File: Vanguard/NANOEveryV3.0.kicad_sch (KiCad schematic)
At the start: 57 parts, among them IC1 MPM3610, J1 -, J2 DNP, Q1 BSS138PS, Q2 BSS138PS, Q3 BSS138, U1 ATMEGA4809, U2 AP2112K-3.3, U3 ATSAMD11D14A, U4 ICM-20602

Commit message: (almost done) with the footprints
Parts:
- FD1, FD2: footprint NANOEveryV3.0:FD-1-1.5 -> TestPoint:TestPoint_THTPad_1.0x1.0mm_Drill0.5mm
- J1: footprint NANOEveryV3.0:ZX62-AB-5PA -> Connector_USB:USB_Micro-AB_Molex_47590-0001
- J2: footprint NANOEveryV3.0:2X03-TP -> Connector_PinHeader_1.00mm:PinHeader_2x03_P1.00mm_Vertical
- JP2: footprint NANOEveryV3.0:1X15-CASTELL -> Connector_PinHeader_1.00mm:PinHeader_1x15_P1.00mm_Vertical_SMD_Pin1Left
- JP3: footprint NANOEveryV3.0:1X15-CASTELL -> Connector_PinHeader_1.00mm:PinHeader_1x15_P1.00mm_Vertical_SMD_Pin1Right
- PB1: footprint NANOEveryV3.0:C&K_PTS820_NO_HOLES -> Button_Switch_SMD:SW_Tactile_SPST_NO_Straight_CK_PTS636Sx25SMTRLFS
- Q1, Q2: footprint NANOEveryV3.0:SOT363 -> Package_TO_SOT_SMD:SOT-363_SC-70-6
- R1, R10, R11, R12, R13, R14, R15, R16, R17, R18, R19, R2, R3, R4, R5, R6, R7, R8, R9: footprint NANOEveryV3.0:0402-1005X55N -> Resistor_SMD:R_0402_1005Metric
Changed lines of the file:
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@@
 			)
 		)
-		(property "Footprint" "NANOEveryV3.0:0402-1005X55N"
+		(property "Footprint" "Resistor_SMD:R_0402_1005Metric"
 			(at 187.96 97.79 0)
 			(effects
@@
 			)
 		)
-		(property "Footprint" "NANOEveryV3.0:0402-1005X55N"
+		(property "Footprint" "Resistor_SMD:R_0402_1005Metric"
 			(at 229.87 146.05 0)
 			(effects
@@
 			)
 		)
-		(property "Footprint" "NANOEveryV3.0:ZX62-AB-5PA"
+		(property "Footprint" "Connector_USB:USB_Micro-AB_Molex_47590-0001"
 			(at 38.1 110.49 0)
 			(effects
@@
 			)
 		)
-		(property "Footprint" "NANOEveryV3.0:FD-1-1.5"
+		(property "Footprint" "TestPoint:TestPoint_THTPad_1.0x1.0mm_Drill0.5mm"
 			(at 396.24 27.94 0)
 			(effects
@@
 			)
 		)
-		(property "Footprint" "NANOEveryV3.0:0402-1005X55N"
+		(property "Footprint" "Resistor_SMD:R_0402_1005Metric"
 			(at 57.15 153.67 0)
 			(effects
@@
 			)
 		)
-		(property "Footprint" "NANOEveryV3.0:FD-1-1.5"
+		(property "Footprint" "TestPoint:TestPoint_THTPad_1.0x1.0mm_Drill0.5mm"
 			(at 389.89 27.94 0)
 			(effects
@@
 			)
 		)
-		(property "Footprint" "NANOEveryV3.0:0402-1005X55N"
+		(property "Footprint" "Resistor_SMD:R_0402_1005Metric"
 			(at 212.09 146.05 0)
 			(effects
@@
 			)
 		)
-		(property "Footprint" "NANOEveryV3.0:0402-1005X55N"
+		(property "Footprint" "Resistor_SMD:R_0402_1005Metric"
 			(at 35.56 49.53 0)
 			(effects
@@
 			)
 		)
-		(property "Footprint" "NANOEveryV3.0:0402-1005X55N"
+		(property "Footprint" "Resistor_SMD:R_0402_1005Metric"
 			(at 229.87 123.19 0)
 			(effects
@@
 			)
 		)
-		(property "Footprint" "NANOEveryV3.0:2X03-TP"
+		(property "Footprint" "Connector_PinHeader_1.00mm:PinHeader_2x03_P1.00mm_Vertical"
 			(at 71.12 152.4 0)
 			(effects
@@
 			)
 		)
-		(property "Footprint" "NANOEveryV3.0:0402-1005X55N"
+		(property "Footprint" "Resistor_SMD:R_0402_1005Metric"
 			(at 248.92 203.2 0)
 			(effects
@@
 			)
 		)
-		(property "Footprint" "NANOEveryV3.0:SOT363"
+		(property "Footprint" "Package_TO_SOT_SMD:SOT-363_SC-70-6"
 			(at 220.98 133.35 0)
 			(effects
@@
 			)
 		)
-		(property "Footprint" "NANOEveryV3.0:0402-1005X55N"
+		(property "Footprint" "Resistor_SMD:R_0402_1005Metric"
 			(at 205.74 97.79 0)
 			(effects
@@
 			)
 		)
-		(property "Footprint" "NANOEveryV3.0:0402-1005X55N"
+		(property "Footprint" "Resistor_SMD:R_0402_1005Metric"
 			(at 50.8 140.97 0)
 			(effects
@@
 			)
 		)
-		(property "Footprint" "NANOEveryV3.0:0402-1005X55N"
+		(property "Footprint" "Resistor_SMD:R_0402_1005Metric"
 			(at 176.53 152.4 0)
 			(effects
@@
 			)
 		)
-		(property "Footprint" "NANOEveryV3.0:1X15-CASTELL"
+		(property "Footprint" "Connector_PinHeader_1.00mm:PinHeader_1x15_P1.00mm_Vertical_SMD_Pin1Left"
 			(at 317.5 99.06 0)
 			(effects
@@
 			)
 		)
-		(property "Footprint" "NANOEveryV3.0:0402-1005X55N"
+		(property "Footprint" "Resistor_SMD:R_0402_1005Metric"
 			(at 35.56 66.04 0)
 			(effects
@@
 			)
 		)
-		(property "Footprint" "NANOEveryV3.0:0402-1005X55N"
+		(property "Footprint" "Resistor_SMD:R_0402_1005Metric"
 			(at 166.37 152.4 0)
 			(effects
@@
 			)
 		)
-		(property "Footprint" "NANOEveryV3.0:0402-1005X55N"
+		(property "Footprint" "Resistor_SMD:R_0402_1005Metric"
 			(at 181.61 123.19 0)
 			(effects
@@
 			)
 		)
-		(property "Footprint" "NANOEveryV3.0:0402-1005X55N"
+		(property "Footprint" "Resistor_SMD:R_0402_1005Metric"
 			(at 73.66 62.23 0)
 			(effects
@@
 			)
 		)
-		(property "Footprint" "NANOEveryV3.0:0402-1005X55N"
+		(property "Footprint" "Resistor_SMD:R_0402_1005Metric"
 			(at 302.26 74.93 0)
 			(effects
@@
 			)
 		)
-		(property "Footprint" "NANOEveryV3.0:0402-1005X55N"
+		(property "Footprint" "Resistor_SMD:R_0402_1005Metric"
 			(at 73.66 54.61 0)
 			(effects
@@
 			)
 		)
-		(property "Footprint" "NANOEveryV3.0:0402-1005X55N"
+		(property "Footprint" "Resistor_SMD:R_0402_1005Metric"
 			(at 80.01 133.35 0)
 			(effects
@@
 			)
 		)
-		(property "Footprint" "NANOEveryV3.0:SOT363"
+		(property "Footprint" "Package_TO_SOT_SMD:SOT-363_SC-70-6"
 			(at 196.85 107.95 0)
 			(effects
@@
 			)
 		)
-		(property "Footprint" "NANOEveryV3.0:1X15-CASTELL"
+		(property "Footprint" "Connector_PinHeader_1.00mm:PinHeader_1x15_P1.00mm_Vertical_SMD_Pin1Right"
 			(at 327.66 99.06 0)
 			(effects
@@
 			)
 		)
-		(property "Footprint" "NANOEveryV3.0:0402-1005X55N"
+		(property "Footprint" "Resistor_SMD:R_0402_1005Metric"
 			(at 212.09 123.19 0)
 			(effects
@@
 			)
 		)
-		(property "Footprint" "NANOEveryV3.0:0402-1005X55N"
+		(property "Footprint" "Resistor_SMD:R_0402_1005Metric"
 			(at 123.19 55.88 0)
 			(effects
@@
 			)
 		)
-		(property "Footprint" "NANOEveryV3.0:C&K_PTS820_NO_HOLES"
+		(property "Footprint" "Button_Switch_SMD:SW_Tactile_SPST_NO_Straight_CK_PTS636Sx25SMTRLFS"
 			(at 236.22 213.36 0)
 			(effects
@@
 			)
 		)
-		(property "Footprint" "NANOEveryV3.0:SOT363"
+		(property "Footprint" "Package_TO_SOT_SMD:SOT-363_SC-70-6"
 			(at 220.98 156.21 0)
 			(effects

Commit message: Assigned footprints for mpm3610
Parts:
- IC1: footprint NANOEveryV3.0:MPM3610 -> Package_DFN_QFN:DFN-18-1EP_3x5mm_P0.5mm_EP1.66x4.4mm
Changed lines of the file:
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@@
 			)
 		)
-		(property "Footprint" "NANOEveryV3.0:MPM3610"
+		(property "Footprint" "Package_DFN_QFN:DFN-18-1EP_3x5mm_P0.5mm_EP1.66x4.4mm"
 			(at 53.34 50.8 0)
 			(effects

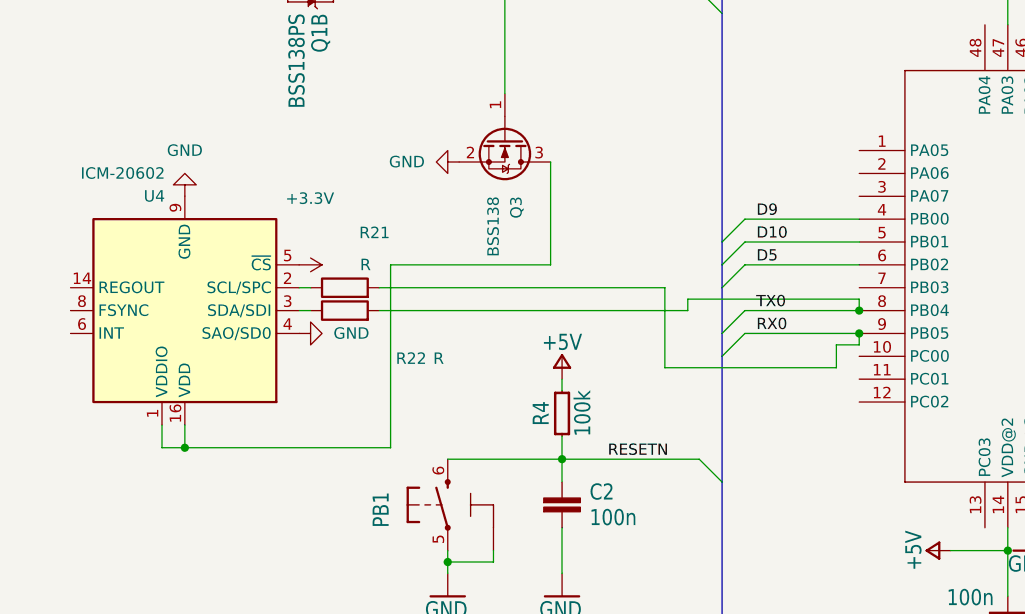
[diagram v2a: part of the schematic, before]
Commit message: Removed connections from icm20602
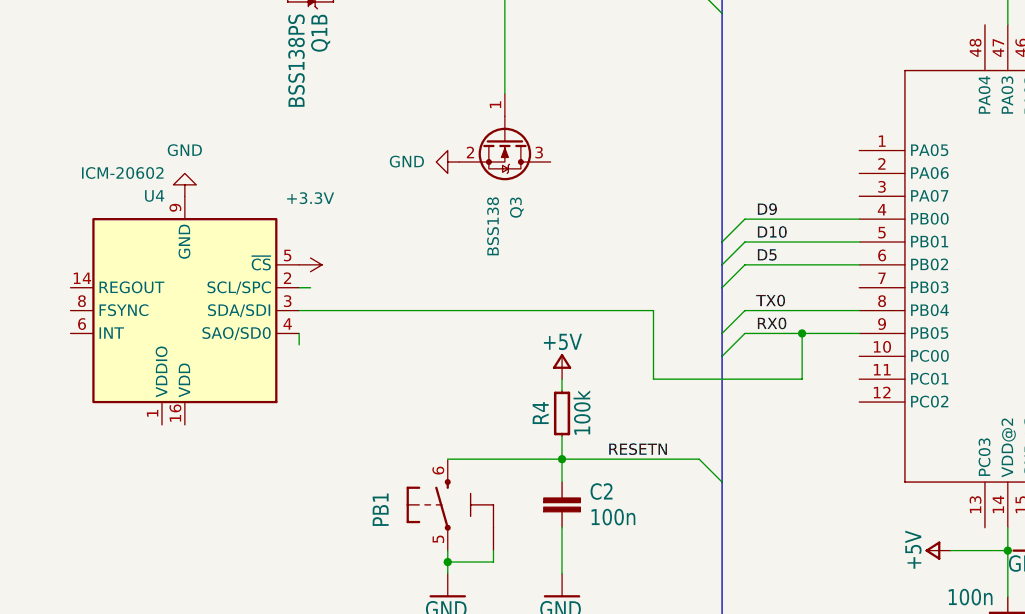
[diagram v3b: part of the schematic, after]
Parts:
- removed R21, R22: R, symbol Device:R
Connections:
- net GND: no longer U4.4 (SAO/SD0)
- net RX0: now also U4.3 (SDA/SDI)
- now unconnected: Q3.3 (D), U4.1 (VDDIO), U4.16 (VDD)

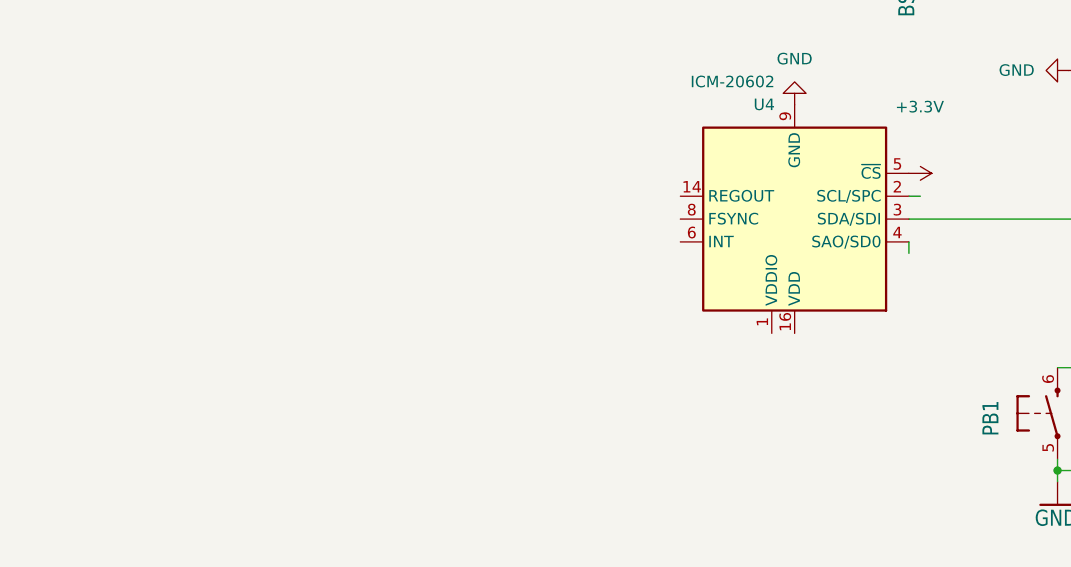
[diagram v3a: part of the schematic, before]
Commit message: Added a Note for icm-20602
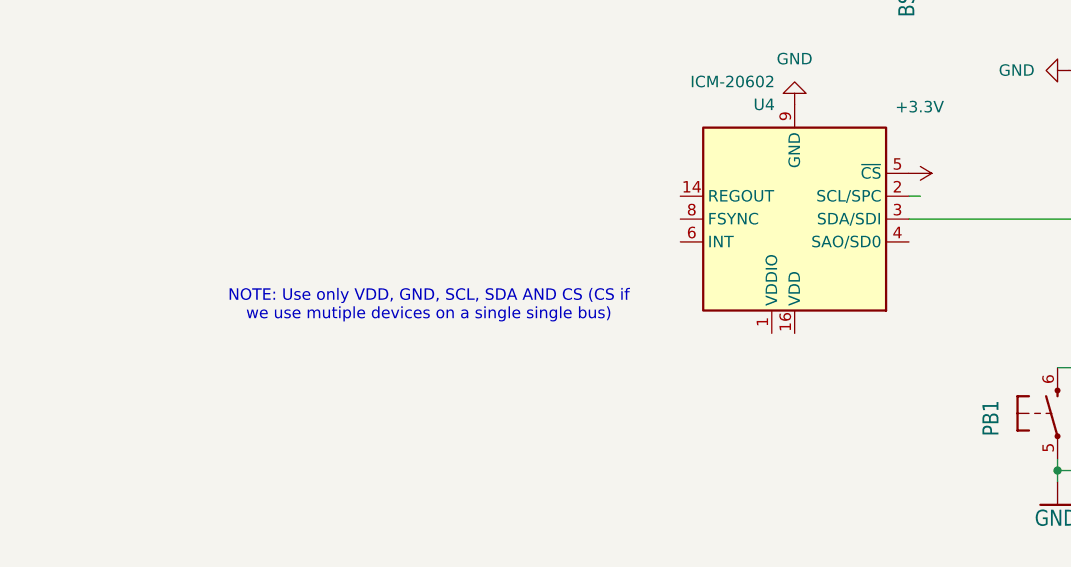
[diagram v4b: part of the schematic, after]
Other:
- note added: "NOTE: Use only VDD, GND, SCL, SDA AND CS (CS if we use mutiple devices on a single single bus)"

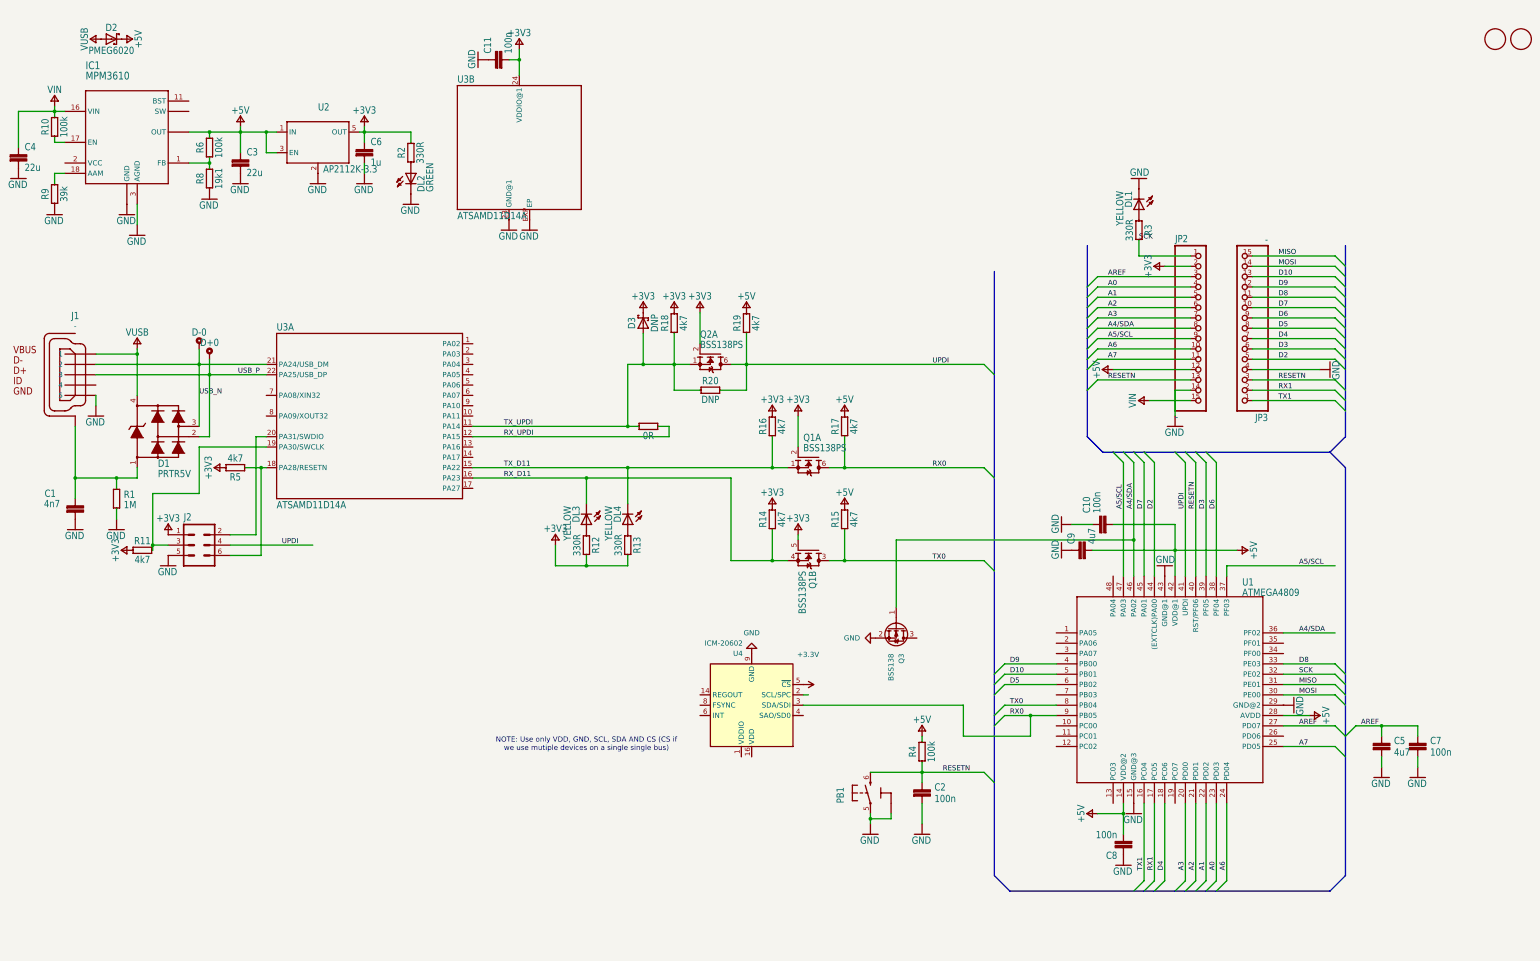
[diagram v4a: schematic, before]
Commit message: micro_SD_card and footprints
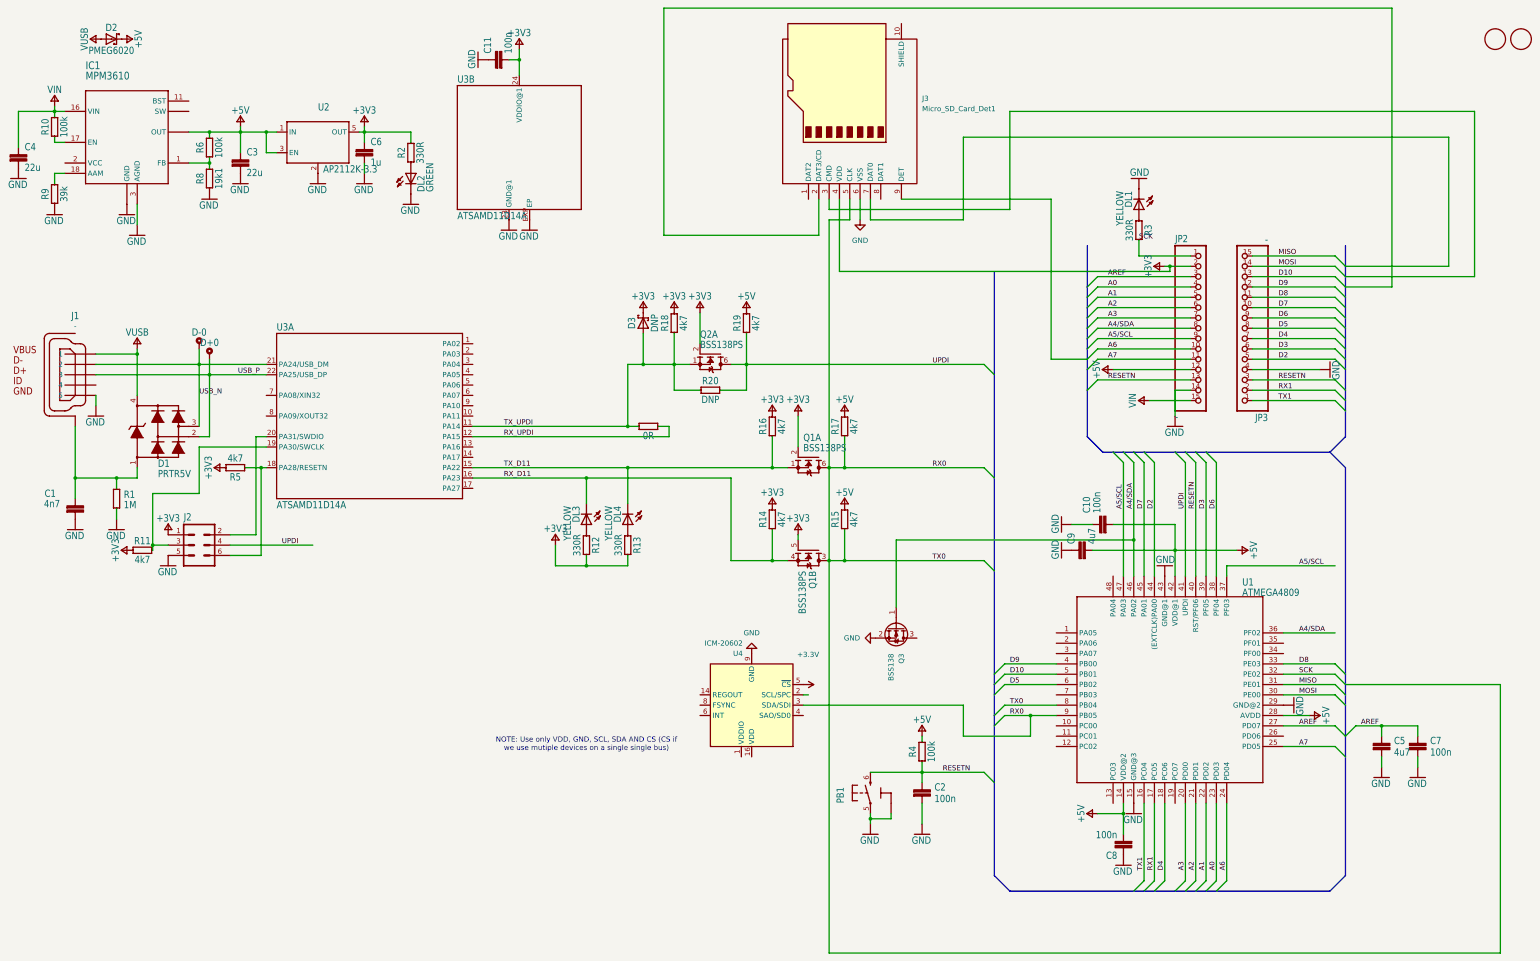
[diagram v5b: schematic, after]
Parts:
- added J3: Micro_SD_Card_Det1, Connector_Card:microSD_HC_Molex_104031-0811, symbol Connector:Micro_SD_Card_Det1
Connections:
- net TX0 is gone; now on net RX0: Q1.3 (D), R15.1, U1.8 (PB04)
- net +3V3: now also J3.4 (VDD)
- net GND: now also J3.6 (VSS)
- net RX0: now also J3.5 (CLK)
